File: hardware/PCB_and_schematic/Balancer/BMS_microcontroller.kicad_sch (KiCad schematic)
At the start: 0 parts

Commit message: Add simulations and recheck schematics + cleanup
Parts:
- added C16, C17, C19, C20: 100n, Capacitor_SMD:C_0805_2012Metric_Pad1.18x1.45mm_HandSolder, symbol Device:C
- added C18: 10u, Capacitor_SMD:CP_Elec_6.3x4.5, symbol Device:C
- added C21: 100n, Resistor_SMD:R_0805_2012Metric_Pad1.20x1.40mm_HandSolder, symbol Device:C
- added D15: 3V3, Diode_SMD:D_MiniMELF, symbol Device:D_Zener
- added D16, D17: D_TVS, Diode_SMD:D_SMC, symbol Device:D_TVS
- added D18, D19, D20, D21: LED, LED_THT:LED_D5.0mm, symbol Device:LED
- added F4: 2A, Fuse:Fuse_2512_6332Metric_Pad1.52x3.35mm_HandSolder, symbol Device:Polyfuse
- added J10: RS485, Connector_PinHeader_2.54mm:PinHeader_1x04_P2.54mm_Vertical, symbol Connector_Generic:Conn_01x04
- added J8: ICP, Connector_PinHeader_2.54mm:PinHeader_1x06_P2.54mm_Vertical, symbol Connector_Generic:Conn_01x06
- added J9: Conn_01x03, Connector_PinHeader_2.54mm:PinHeader_1x03_P2.54mm_Vertical, symbol Connector_Generic:Conn_01x03
- added MOD1: LM2596-Step-Down, My-Footprints:MP1504_Mini_3A_Step_Down_Conv, symbol My-Lib:LM2596-Step-Down
- added Q17, Q18, Q19, Q20: BC817, Package_TO_SOT_SMD:SOT-23, symbol Transistor_BJT:BC817
- added R46, R53, R54: 10k, Resistor_SMD:R_0805_2012Metric_Pad1.20x1.40mm_HandSolder, symbol Device:R
- added R47: 6k8, Resistor_SMD:R_0805_2012Metric_Pad1.20x1.40mm_HandSolder, symbol Device:R
- added R48: 1k3, Resistor_SMD:R_0805_2012Metric_Pad1.20x1.40mm_HandSolder, symbol Device:R
- added R49: 1k, Resistor_SMD:R_0805_2012Metric_Pad1.20x1.40mm_HandSolder, symbol Device:R
- added R50, R52: 510R, Resistor_SMD:R_0805_2012Metric_Pad1.20x1.40mm_HandSolder, symbol Device:R
- added R51: 120R, Resistor_SMD:R_0805_2012Metric_Pad1.20x1.40mm_HandSolder, symbol Device:R
- added R55, R57, R59, R61: 10K, Resistor_SMD:R_0805_2012Metric_Pad1.20x1.40mm_HandSolder, symbol Device:R
- added R56, R58, R60, R62: 220R, Resistor_SMD:R_0805_2012Metric_Pad1.20x1.40mm_HandSolder, symbol Device:R
- added U4: PIC16F886-IP, Package_SO:SOIC-28W_7.5x17.9mm_P1.27mm, symbol MCU_Microchip_PIC16:PIC16F886-IP
- added U5: TL431LP, Package_TO_SOT_THT:TO-92_Inline, symbol Reference_Voltage:TL431LP
- added U6: ST485, Package_SO:SOIC-8_3.9x4.9mm_P1.27mm, symbol Interface_UART:ST485EBDR
- added U7: INA226, Package_SO:VSSOP-10_3x3mm_P0.5mm, symbol Sensor_Energy:INA226
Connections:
- new net: D20.2 (A), R60.2
- new net: Q20.3 (C), R62.1
- new net: D21.2 (A), R62.2
- new net: D18.2 (A), R56.2
- new net: Q17.3 (C), R56.1
- new net: Q18.1 (B), R57.1
- new net: Q19.1 (B), R59.1
- new net: Q19.3 (C), R60.1
- new net: Q20.1 (B), R61.1
- new net: F4.1, MOD1.4 (OUT+)
- new net: Q18.3 (C), R58.1
- new net: D19.2 (A), R58.2
- new net: Q17.1 (B), R55.1
- new net +5V: C16.1, C18.2, C20.1, C21.1, D18.1 (K), D19.1 (K), D20.1 (K), D21.1 (K), F4.2, J10.1 (Pin_1), J8.2 (Pin_2), J9.2 (Pin_2), R46.1, R49.1, R50.1, R53.1, R54.1, U4.20 (VDD), U6.8 (VCC), U7.6 (VS)
- new net +BATT_12V: R47.1
- new net +BATT_24V: MOD1.2 (IN+), U7.8 (Vbus), U7.9 (Vin-)
- new net BALANCE_ON_12V: U4.25 (P1D/AN11/RB4)
- new net BALANCE_ON_24V: U4.26 (~{T1G}/AN13/RB5)
- new net CLOCK: R54.2, U4.14 (RC3/SCK/SCL), U7.5 (SCL)
- new net DBG_UART: J8.6 (Pin_6), U4.6 (T0CKI/C1OUT/RA4)
- new net GND: C16.2, C17.2, C18.1, C19.2, C20.2, C21.2, D15.2 (A), D16.1 (A1), D17.1 (A1), J10.4 (Pin_4), J8.3 (Pin_3), J9.3 (Pin_3), MOD1.1 (IN-), MOD1.3 (OUT-), Q17.2 (E), Q18.2 (E), Q19.2 (E), Q20.2 (E), R48.2, R52.2, U4.19 (VSS), U4.8 (VSS), U5.2 (A), U6.5 (GND), U7.1 (A1), U7.2 (A0), U7.7 (GND)
- new net IDEAL_DIODE_DISABLE: U4.9 (CLKIN/OSC1/RA7)
- new net LED1: R55.2, U4.24 (PGM/C12IN2-/AN8/RB3)
- new net LED2: R57.2, U4.23 (P1B/AN8/RB2)
- new net PGC: J8.5 (Pin_5), R61.2, U4.27 (ICSPCLK/RB6)
- new net PGD: J8.4 (Pin_4), R59.2, U4.28 (ICSPDAT/RB7)
- new net PWM_OUT1: U4.21 (INT/AN12/RB0)
- new net PWM_OUT2: U4.22 (P1C/AN10/RB1)
- new net PWM_OUT_CHRG: U4.13 (RC2/P1A/CCP1)
- new net PWM_OUT_DISCH: U4.12 (RC1/T1OSI/CCP2)
- new net RB1: J9.1 (Pin_1)
- new net RS232_RX: U4.18 (RC7/RX/DT), U6.1 (RO)
- new net RS232_TX: U4.17 (RC6/TX/CK), U6.4 (DI)
- new net RS485_A: D16.2 (A2), J10.3 (Pin_3), R51.2, R52.1, U6.6 (A)
- new net RS485_B: D17.2 (A2), J10.2 (Pin_2), R50.2, R51.1, U6.7 (B)
- new net RS485_OUTPUT_ENABLE: U4.16 (RC5/SDO), U6.2 (~{RE}), U6.3 (DE)
- new net RST: J8.1 (Pin_1), R46.2, U4.1 (RE3/~{MCLR}/Vpp)
- new net R_shunt: U7.10 (Vin+)
- new net SDA: R53.2, U4.15 (RC4/SDI/SDA), U7.4 (SDA)
- new net TEMP_AKU_12V: U4.7 (~{SS}/C2OUT/AN4/RA5)
- new net TEMP_AKU_24V: U4.10 (CLKOUT/OSC2/RA6)
- new net TEMP_HEAT_SINK_12V: U4.3 (C12IN1-/AN1/RA1)
- new net TEMP_HEAT_SINK_24V: U4.4 (CVref/C2IN1+/Vref-/AN2/RA2)
- new net VOLTAGE_BATT_12V: C17.1, D15.1 (K), R47.2, R48.1, U4.2 (ULPWU/C12IN0-/AN0/RA0)
- new net VREF_2V5: C19.1, R49.2, U4.5 (C1IN+/Vref+/AN3/RA3), U5.1 (REF), U5.3 (K)
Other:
- note added: "/RE - Receiver Output Enable Active LOW"
- note added: "DC converter VBAT -> 5V"
- note added: "INA226"
- note added: "PIC16F886"
- note added: "ST485"
- note added: "STATUS DIODES"

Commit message: Chceck and update DC module and meter probe pcb
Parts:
- renumbered R46 to R47, R47 to R48, R48 to R49, R49 to R50, R50 to R51, R51 to R52, R52 to R53, R53 to R54, R54 to R55, R55 to R56, R56 to R57, R57 to R58, R58 to R59, R59 to R60, R60 to R61, R61 to R62, R62 to R63
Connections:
- net RB1 is gone; now on net RC0: J9.1 (Pin_1)
- net RC0: now reaches U4.11 (RC0/T1OSO/T1CK1)

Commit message: Routing balancer pcb
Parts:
- U5: footprint Package_TO_SOT_THT:TO-92_Inline -> My-Footprints:TO-92_Inline_Wide
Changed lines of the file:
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@@
 			)
 		)
-		(property "Footprint" "Package_TO_SOT_THT:TO-92_Inline"
+		(property "Footprint" "My-Footprints:TO-92_Inline_Wide"
 			(at 110.49 125.73 0)
 			(effects

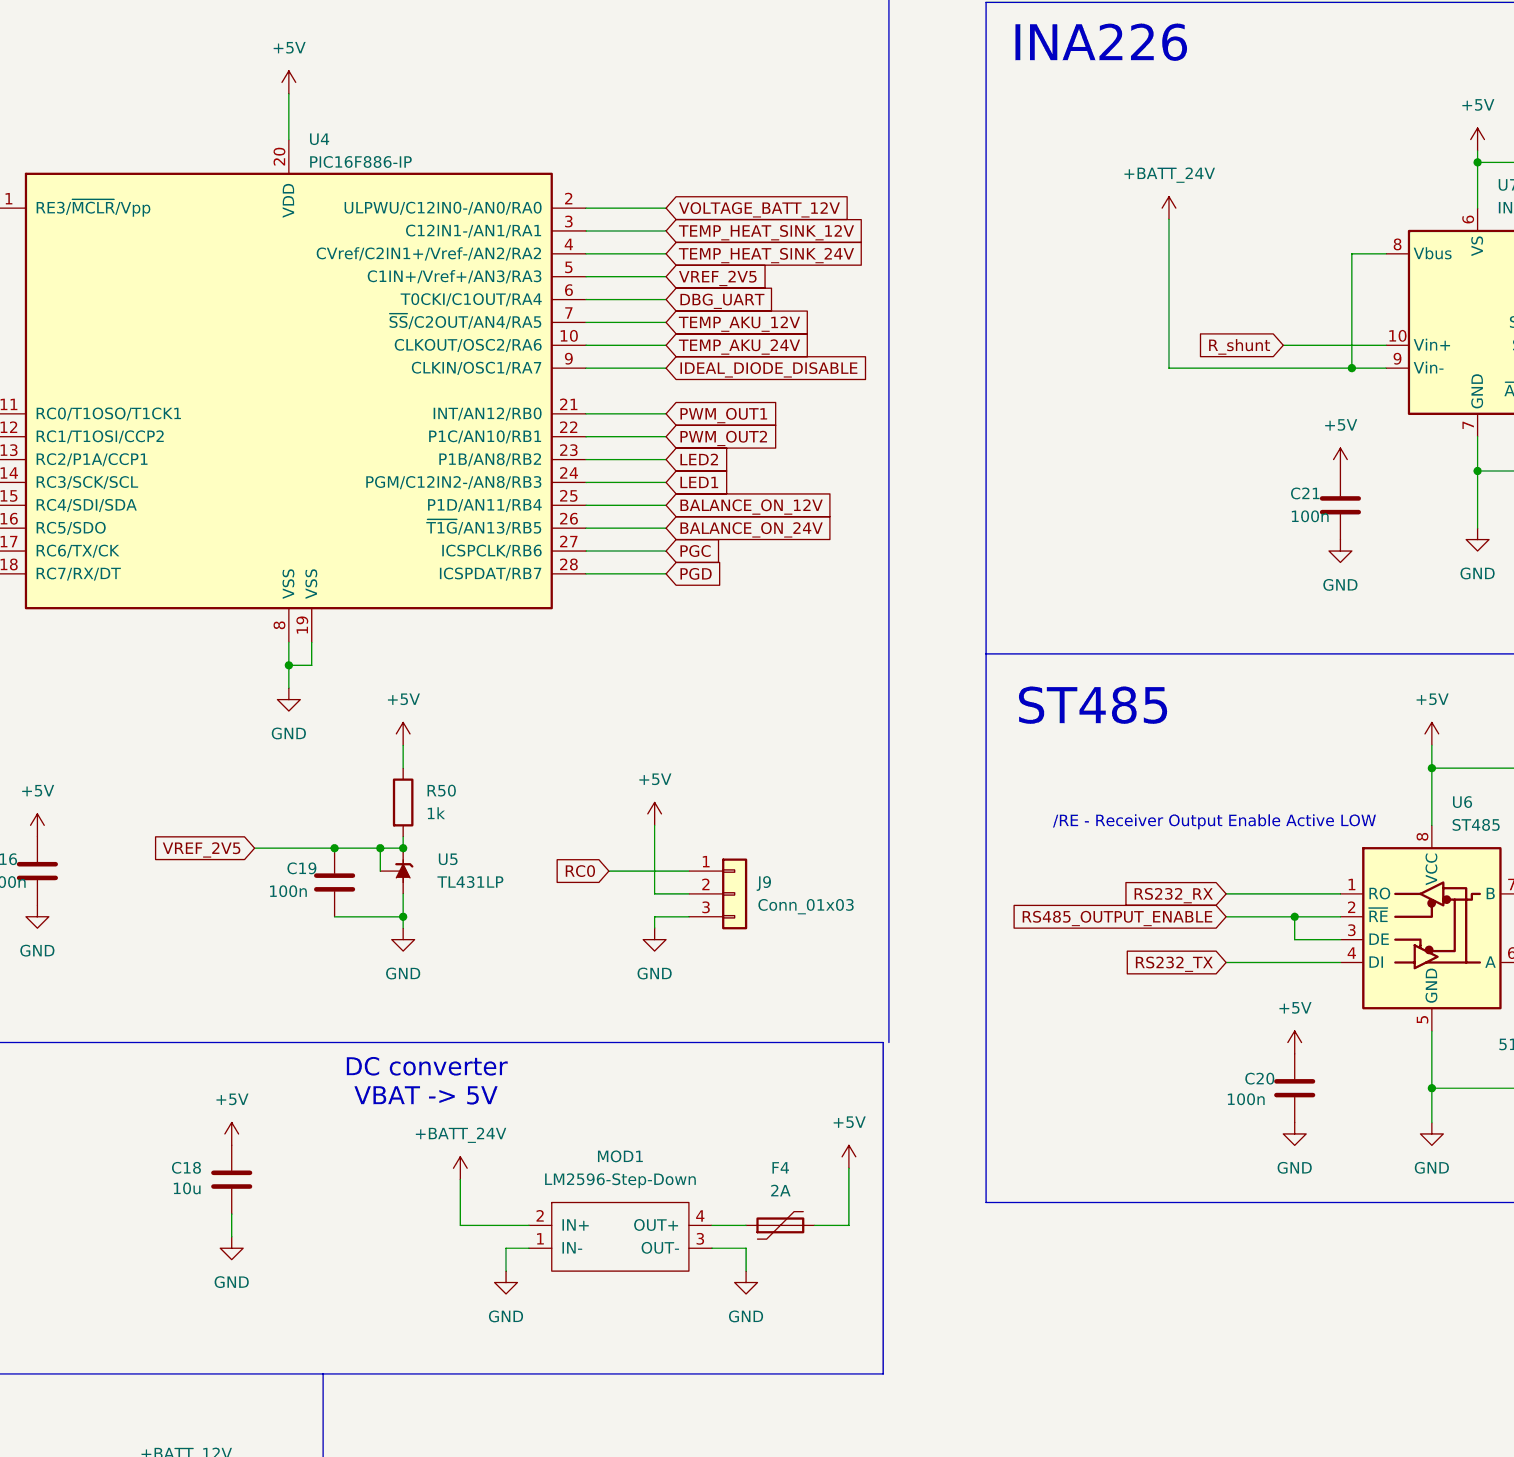
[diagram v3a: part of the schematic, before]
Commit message: Splitter and connector footprints, progress with balancer pcb routing
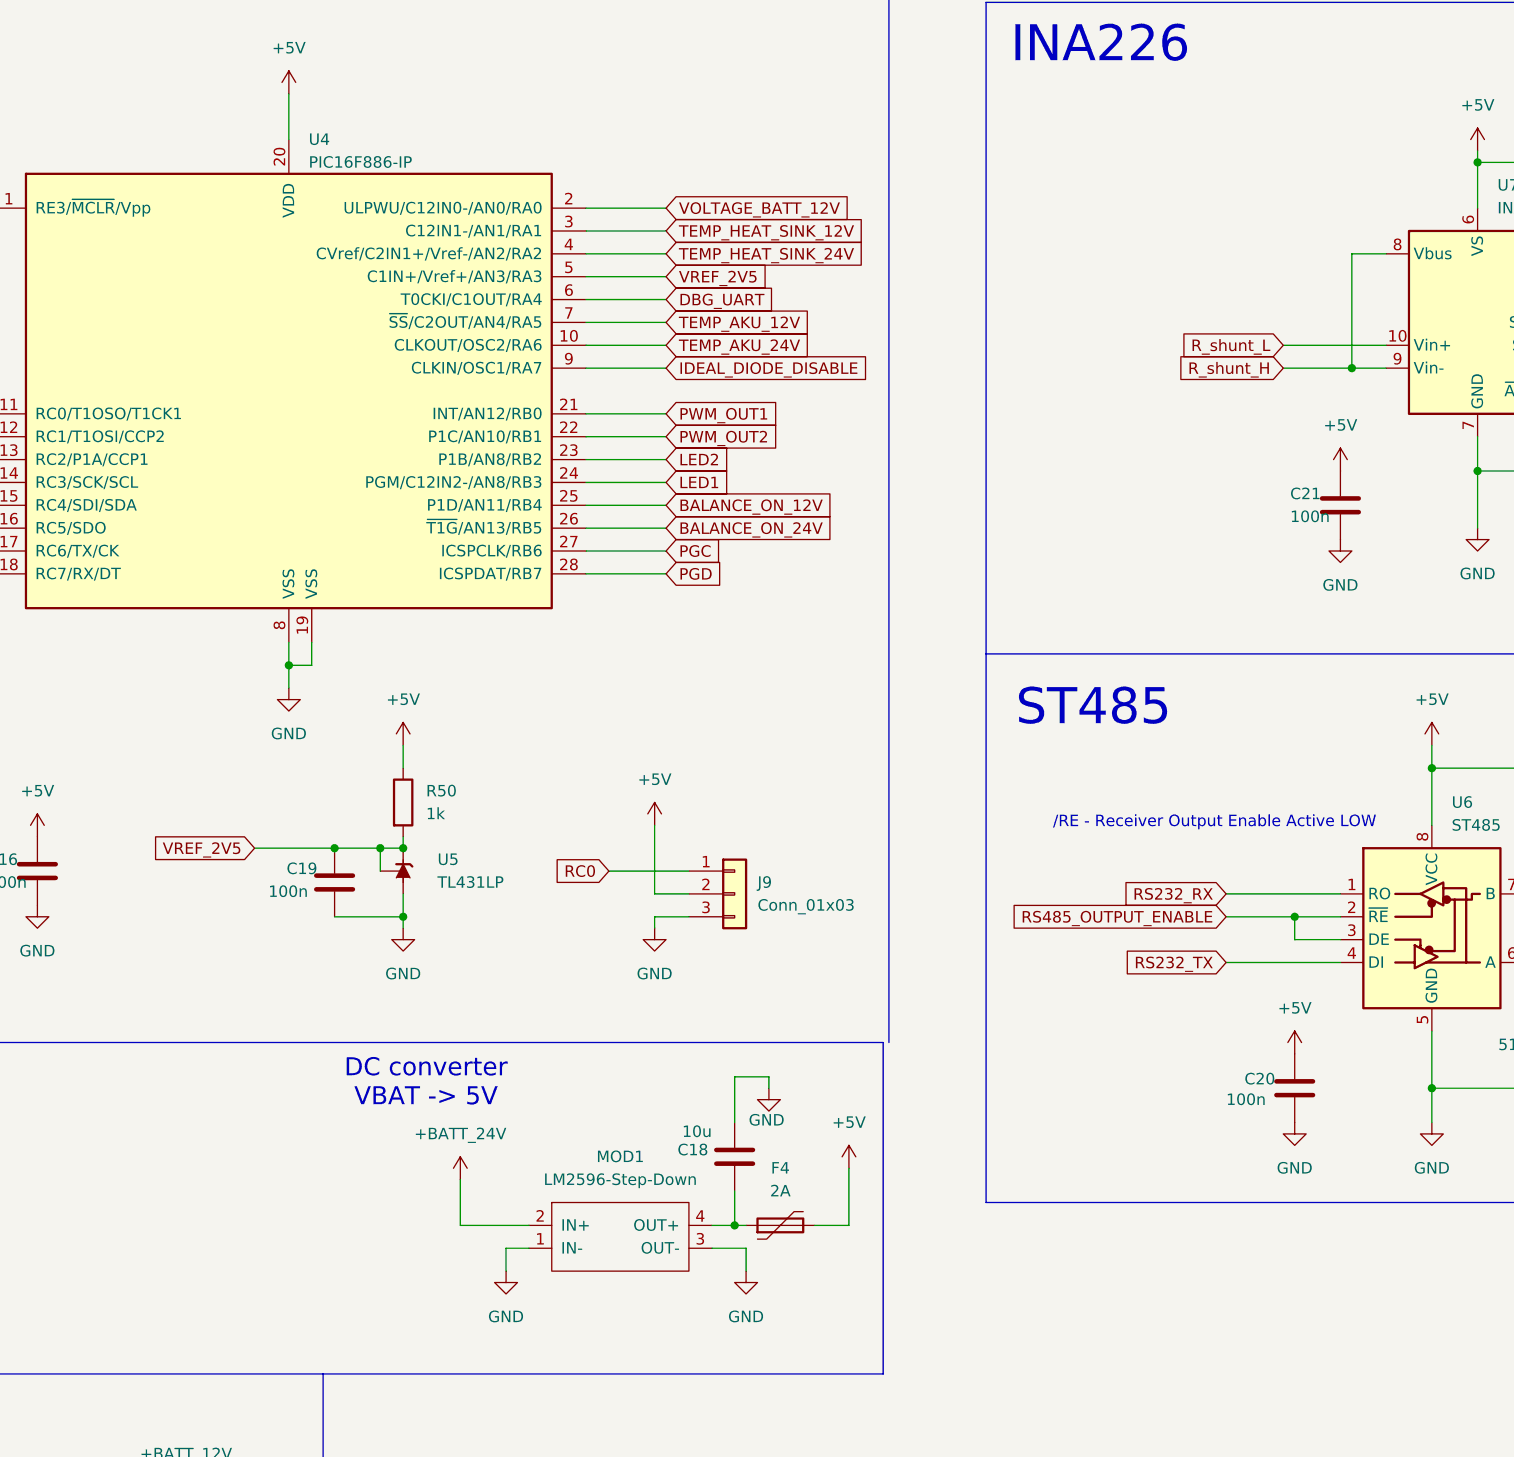
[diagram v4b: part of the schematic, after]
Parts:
- C18: footprint Capacitor_SMD:CP_Elec_6.3x4.5 -> Capacitor_THT:CP_Radial_D6.3mm_P2.50mm
- MOD1: footprint My-Footprints:MP1504_Mini_3A_Step_Down_Conv -> My-Footprints-converters-modules:MP1584_Mini_3A_Step_Down_Conv
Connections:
- net +5V: no longer C18.2
- net +BATT_24V: no longer U7.8 (Vbus), U7.9 (Vin-)
- net at F4.1, MOD1.4 (OUT+): now also C18.2
- net R_shunt renamed R_shunt_L
- new net R_shunt_H: U7.8 (Vbus), U7.9 (Vin-)
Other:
- moved on the sheet: C18
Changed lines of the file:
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@@
 	)
 	(junction
-		(at 212.09 69.85)
+		(at 99.06 123.19)
 		(diameter 0)
 		(color 0 0 0 0)
 	)
 	(junction
-		(at 99.06 123.19)
+		(at 104.14 123.19)
 		(diameter 0)
 		(color 0 0 0 0)
 	)
 	(junction
-		(at 104.14 123.19)
+		(at 143.51 165.1)
 		(diameter 0)
 		(color 0 0 0 0)
@@
 	)
 	(junction
+		(at 212.09 69.85)
+		(diameter 0)
+		(color 0 0 0 0)
+	)
+	(junction
 		(at 205.74 130.81)
 		(diameter 0)
@@
 	(wire
 		(pts
+			(xy 147.32 148.59) (xy 143.51 148.59)
+		)
+		(stroke
+			(width 0)
+			(type default)
+		)
+	)
+	(wire
+		(pts
 			(xy 212.09 69.85) (xy 215.9 69.85)
 		)
@@
 	(wire
 		(pts
-			(xy 191.77 69.85) (xy 212.09 69.85)
-		)
-		(stroke
-			(width 0)
-			(type default)
-		)
-	)
-	(wire
-		(pts
 			(xy 226.06 46.99) (xy 248.92 46.99)
 		)
@@
 		)
 	)
+	(wire
+		(pts
+			(xy 204.47 69.85) (xy 212.09 69.85)
+		)
+		(stroke
+			(width 0)
+			(type default)
+		)
+	)
 	(polyline
 		(pts
@@
 	(wire
 		(pts
+			(xy 143.51 148.59) (xy 143.51 153.67)
+		)
+		(stroke
+			(width 0)
+			(type default)
+		)
+	)
+	(wire
+		(pts
 			(xy 127 85.09) (xy 135.89 85.09)
 		)
@@
 	(wire
 		(pts
-			(xy 87.63 163.83) (xy 87.63 166.37)
+			(xy 147.32 148.59) (xy 147.32 149.86)
 		)
 		(stroke
@@
 	(wire
 		(pts
-			(xy 191.77 69.85) (xy 191.77 53.34)
-		)
-		(stroke
-			(width 0)
-			(type default)
-		)
-	)
-	(wire
-		(pts
 			(xy 231.14 135.89) (xy 234.95 135.89)
 		)
@@
 		)
 	)
+	(wire
+		(pts
+			(xy 143.51 161.29) (xy 143.51 165.1)
+		)
+		(stroke
+			(width 0)
+			(type default)
+		)
+	)
 	(polyline
 		(pts
@@
 	(wire
 		(pts
-			(xy 140.97 165.1) (xy 144.78 165.1)
+			(xy 140.97 165.1) (xy 143.51 165.1)
 		)
 		(stroke
@@
 	(wire
 		(pts
+			(xy 143.51 165.1) (xy 144.78 165.1)
+		)
+		(stroke
+			(width 0)
+			(type default)
+		)
+	)
+	(wire
+		(pts
 			(xy 234.95 147.32) (xy 234.95 149.86)
 		)
@@
 		)
 	)
-	(global_label "R_shunt"
+	(global_label "R_shunt_L"
 		(shape input)
 		(at 204.47 67.31 180)
@@
 		)
 		(property "Intersheetrefs" "${INTERSHEET_REFS}"
-			(at 194.0464 67.31 0)
+			(at 192.0507 67.31 0)
 			(effects
 				(font
@@
 		)
 	)
+	(global_label "R_shunt_H"
+		(shape input)
+		(at 204.47 69.85 180)
+		(fields_autoplaced yes)
+		(effects
+			(font
+				(size 1.27 1.27)
+			)
+			(justify right)
+		)
+		(property "Intersheetrefs" "${INTERSHEET_REFS}"
+			(at 191.7483 69.85 0)
+			(effects
+				(font
+					(size 1.27 1.27)
+				)
+				(justify right)
+				(hide yes)
+			)
+		)
+	)
 	(global_label "VOLTAGE_BATT_12V"
 		(shape input)
@@
 	(symbol
 		(lib_id "Device:C")
-		(at 87.63 160.02 180)
+		(at 143.51 157.48 0)
 		(unit 1)
 		(exclude_from_sim no)
@@
 		(dnp no)
 		(property "Reference" "C18"
-			(at 84.328 158.75 0)
+			(at 137.16 156.718 0)
 			(effects
 				(font
@@
 		)
 		(property "Value" "10u"
-			(at 84.328 161.036 0)
+			(at 137.668 154.686 0)
 			(effects
 				(font
@@
 			)
 		)
-		(property "Footprint" "Capacitor_SMD:CP_Elec_6.3x4.5"
-			(at 86.6648 156.21 0)
+		(property "Footprint" "Capacitor_THT:CP_Radial_D6.3mm_P2.50mm"
+			(at 144.4752 161.29 0)
 			(effects
 				(font
@@
 		)
 		(property "Datasheet" "~"
-			(at 87.63 160.02 0)
+			(at 143.51 157.48 0)
 			(effects
 				(font
@@
 		)
 		(property "Description" "Unpolarized capacitor"
-			(at 87.63 160.02 0)
+			(at 143.51 157.48 0)
 			(effects
 				(font
@@
 	)
 	(symbol
-		(lib_id "power:+BATT")
-		(at 191.77 53.34 0)
-		(unit 1)
-		(exclude_from_sim no)
-		(in_bom yes)
-		(on_board yes)
-		(dnp no)
-		(fields_autoplaced yes)
-		(property "Reference" "#PWR071"
-			(at 191.77 57.15 0)
-			(effects
-				(font
-					(size 1.27 1.27)
-				)
-				(hide yes)
-			)
-		)
-		(property "Value" "+BATT_24V"
-			(at 191.77 48.26 0)
-			(effects
-				(font
-					(size 1.27 1.27)
-				)
-			)
-		)
-		(property "Footprint" ""
-			(at 191.77 53.34 0)
-			(effects
-				(font
-					(size 1.27 1.27)
-				)
-				(hide yes)
-			)
-		)
-		(property "Datasheet" ""
-			(at 191.77 53.34 0)
-			(effects
-				(font
-					(size 1.27 1.27)
-				)
-				(hide yes)
-			)
-		)
-		(property "Description" "Power symbol creates a global label with name \"+BATT\""
-			(at 191.77 53.34 0)
-			(effects
-				(font
-					(size 1.27 1.27)
-				)
-				(hide yes)
-			)
-		)
-		(pin "1"
-		)
-		(instances
-			(project "Balancer"
-				(path "/555ba40f-9abb-4b99-82c6-07e888fda9fd/3b90ff07-e5cb-404b-939d-de320e975ba1"
-					(reference "#PWR071")
-					(unit 1)
-				)
-			)
-		)
-	)
-	(symbol
 		(lib_id "power:GND")
 		(at 43.18 137.16 0)
@@
 	)
 	(symbol
-		(lib_id "power:+5V")
-		(at 87.63 156.21 0)
-		(unit 1)
-		(exclude_from_sim no)
-		(in_bom yes)
-		(on_board yes)
-		(dnp no)
-		(fields_autoplaced yes)
-		(property "Reference" "#PWR059"
-			(at 87.63 160.02 0)
-			(effects
-				(font
-					(size 1.27 1.27)
-				)
-				(hide yes)
-			)
-		)
-		(property "Value" "+5V"
-			(at 87.63 151.13 0)
-			(effects
-				(font
-					(size 1.27 1.27)
-				)
-			)
-		)
-		(property "Footprint" ""
-			(at 87.63 156.21 0)
-			(effects
-				(font
-					(size 1.27 1.27)
-				)
-				(hide yes)
-			)
-		)
-		(property "Datasheet" ""
-			(at 87.63 156.21 0)
-			(effects
-				(font
-					(size 1.27 1.27)
-				)
-				(hide yes)
-			)
-		)
-		(property "Description" "Power symbol creates a global label with name \"+5V\""
-			(at 87.63 156.21 0)
-			(effects
-				(font
-					(size 1.27 1.27)
-				)
-				(hide yes)
-			)
-		)
-		(pin "1"
-		)
-		(instances
-			(project "Balancer"
-				(path "/555ba40f-9abb-4b99-82c6-07e888fda9fd/3b90ff07-e5cb-404b-939d-de320e975ba1"
-					(reference "#PWR059")
-					(unit 1)
-				)
-			)
-		)
-	)
-	(symbol
 		(lib_id "Device:R")
 		(at 256.54 57.15 0)
@@
 			)
 		)
-		(property "Footprint" "My-Footprints:MP1504_Mini_3A_Step_Down_Conv"
+		(property "Footprint" "My-Footprints-converters-modules:MP1584_Mini_3A_Step_Down_Conv"
 			(at 130.81 158.75 0)
 			(effects
@@
 	(symbol
 		(lib_id "power:GND")
-		(at 87.63 166.37 0)
+		(at 147.32 149.86 0)
 		(unit 1)
 		(exclude_from_sim no)
@@
 		(on_board yes)
 		(dnp no)
-		(fields_autoplaced yes)
 		(property "Reference" "#PWR060"
-			(at 87.63 172.72 0)
+			(at 147.32 156.21 0)
 			(effects
 				(font
@@
 		)
 		(property "Value" "GND"
-			(at 87.63 171.45 0)
+			(at 147.066 153.416 0)
 			(effects
 				(font
@@
 		)
 		(property "Footprint" ""
-			(at 87.63 166.37 0)
+			(at 147.32 149.86 0)
 			(effects
 				(font
@@
 		)
 		(property "Datasheet" ""
-			(at 87.63 166.37 0)
+			(at 147.32 149.86 0)
 			(effects
 				(font
@@
 		)
 		(property "Description" "Power symbol creates a global label with name \"GND\" , ground"
-			(at 87.63 166.37 0)
+			(at 147.32 149.86 0)
 			(effects
 				(font
